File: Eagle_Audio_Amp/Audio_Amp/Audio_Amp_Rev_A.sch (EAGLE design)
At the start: 1 part, among them IC1 LM386M-1

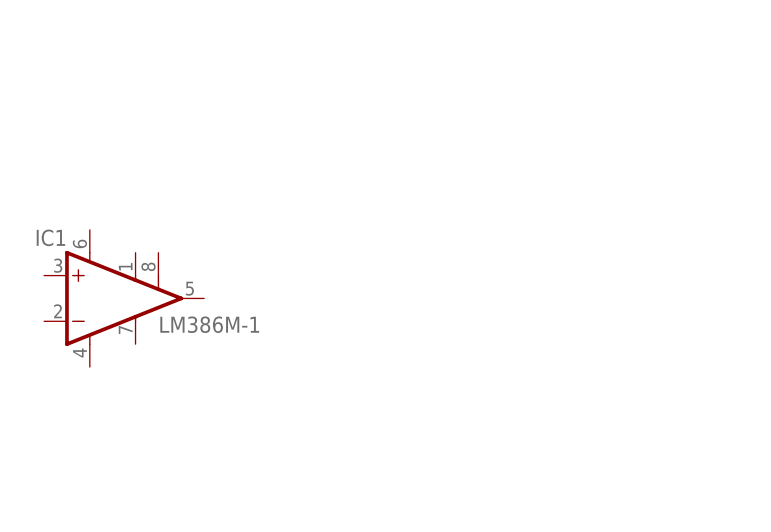
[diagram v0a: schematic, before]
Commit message: Add basic LM386 circuit with bass boost
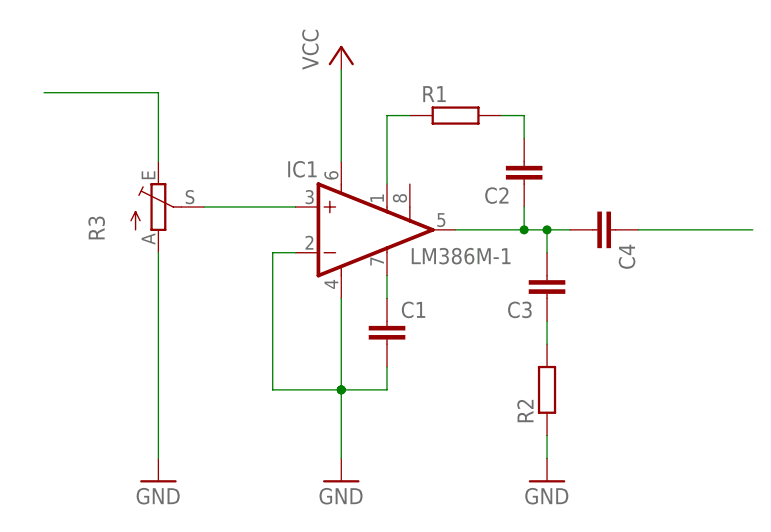
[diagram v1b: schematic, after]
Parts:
- added C1, C2, C3, C4: (no value), rcl:C-EUC0805
- added R1, R2: (no value), rcl:R-EU_R0805
- added R3: (no value), pot:TRIM_EU-CIP20C-6MM
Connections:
- new net GND: C1.2, IC1.-IN, IC1.GND, R2.1, R3.A
- new net N$1: C1.1, IC1.BYPASS
- new net N$2: IC1.+IN, R3.S
- new net N$3: C2.1, C3.2, C4.2, IC1.OUT
- new net N$4: IC1.GAIN@1, R1.1
- new net N$5: C2.2, R1.2
- new net N$6: C3.1, R2.2
- new net N$7: C4.1
- new net N$8: R3.E
- new net VCC: IC1.VS
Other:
- moved on the sheet: IC1
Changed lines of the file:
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@@
 <setting verticaltext="up"/>
 </settings>
-<grid distance="0.1" unitdist="inch" unit="inch" style="lines" multiple="1" display="no" altdistance="0.01" altunitdist="inch" altunit="inch"/>
+<grid distance="0.1" unitdist="inch" unit="inch" style="lines" multiple="1" display="yes" altdistance="0.01" altunitdist="inch" altunit="inch"/>
 <layers>
 <layer number="1" name="Top" color="4" fill="1" visible="no" active="no"/>
@@
 <parts>
 <part name="IC1" library="linear" deviceset="LM386?-*" device="M" technology="1"/>
+<part name="R1" library="rcl" deviceset="R-EU_" device="R0805"/>
+<part name="C1" library="rcl" deviceset="C-EU" device="C0805"/>
+<part name="C2" library="rcl" deviceset="C-EU" device="C0805"/>
+<part name="C3" library="rcl" deviceset="C-EU" device="C0805"/>
+<part name="C4" library="rcl" deviceset="C-EU" device="C0805"/>
+<part name="GND1" library="supply1" deviceset="GND" device=""/>
+<part name="GND2" library="supply1" deviceset="GND" device=""/>
+<part name="P+1" library="supply1" deviceset="VCC" device=""/>
+<part name="R3" library="pot" deviceset="TRIM_EU-" device="CIP20C-6MM"/>
+<part name="R2" library="rcl" deviceset="R-EU_" device="R0805"/>
+<part name="GND4" library="supply1" deviceset="GND" device=""/>
 </parts>
 <sheets>
@@
 </plain>
 <instances>
-<instance part="IC1" gate="G$1" x="63.5" y="48.26"/>
+<instance part="IC1" gate="G$1" x="91.44" y="55.88"/>
+<instance part="R1" gate="G$1" x="101.6" y="68.58"/>
+<instance part="C1" gate="G$1" x="93.98" y="45.72"/>
+<instance part="C2" gate="G$1" x="109.22" y="60.96" rot="R180"/>
+<instance part="C3" gate="G$1" x="111.76" y="48.26" rot="R180"/>
+<instance part="C4" gate="G$1" x="119.38" y="55.88" rot="R270"/>
+<instance part="GND1" gate="1" x="68.58" y="27.94"/>
+<instance part="GND2" gate="1" x="88.9" y="27.94"/>
+<instance part="P+1" gate="VCC" x="88.9" y="76.2"/>
+<instance part="R3" gate="1" x="68.58" y="58.42"/>
+<instance part="R2" gate="G$1" x="111.76" y="38.1" rot="R90"/>
+<instance part="GND4" gate="1" x="111.76" y="27.94"/>
 </instances>
 <busses>
 </busses>
 <nets>
+<net name="N$2" class="0">
+<segment>
+<pinref part="IC1" gate="G$1" pin="+IN"/>
+<wire x1="83.82" y1="58.42" x2="73.66" y2="58.42" width="0.1524" layer="91"/>
+<pinref part="R3" gate="1" pin="S"/>
+</segment>
+</net>
+<net name="GND" class="0">
+<segment>
+<pinref part="IC1" gate="G$1" pin="-IN"/>
+<wire x1="83.82" y1="53.34" x2="81.28" y2="53.34" width="0.1524" layer="91"/>
+<wire x1="81.28" y1="53.34" x2="81.28" y2="38.1" width="0.1524" layer="91"/>
+<wire x1="81.28" y1="38.1" x2="88.9" y2="38.1" width="0.1524" layer="91"/>
+<pinref part="IC1" gate="G$1" pin="GND"/>
+<wire x1="88.9" y1="38.1" x2="88.9" y2="48.26" width="0.1524" layer="91"/>
+<pinref part="GND2" gate="1" pin="GND"/>
+<wire x1="88.9" y1="30.48" x2="88.9" y2="38.1" width="0.1524" layer="91"/>
+<junction x="88.9" y="38.1"/>
+<wire x1="93.98" y1="38.1" x2="88.9" y2="38.1" width="0.1524" layer="91"/>
+<junction x="88.9" y="38.1"/>
+<pinref part="C1" gate="G$1" pin="2"/>
+<wire x1="93.98" y1="40.64" x2="93.98" y2="38.1" width="0.1524" layer="91"/>
+</segment>
+<segment>
+<pinref part="R2" gate="G$1" pin="1"/>
+<pinref part="GND4" gate="1" pin="GND"/>
+<wire x1="111.76" y1="33.02" x2="111.76" y2="30.48" width="0.1524" layer="91"/>
+</segment>
+<segment>
+<pinref part="GND1" gate="1" pin="GND"/>
+<pinref part="R3" gate="1" pin="A"/>
+<wire x1="68.58" y1="30.48" x2="68.58" y2="53.34" width="0.1524" layer="91"/>
+</segment>
+</net>
+<net name="N$1" class="0">
+<segment>
+<pinref part="IC1" gate="G$1" pin="BYPASS"/>
+<pinref part="C1" gate="G$1" pin="1"/>
+<wire x1="93.98" y1="50.8" x2="93.98" y2="48.26" width="0.1524" layer="91"/>
+</segment>
+</net>
+<net name="N$3" class="0">
+<segment>
+<pinref part="IC1" gate="G$1" pin="OUT"/>
+<wire x1="101.6" y1="55.88" x2="109.22" y2="55.88" width="0.1524" layer="91"/>
+<pinref part="C2" gate="G$1" pin="1"/>
+<wire x1="109.22" y1="55.88" x2="109.22" y2="58.42" width="0.1524" layer="91"/>
+<pinref part="C4" gate="G$1" pin="2"/>
+<wire x1="109.22" y1="55.88" x2="111.76" y2="55.88" width="0.1524" layer="91"/>
+<junction x="109.22" y="55.88"/>
+<pinref part="C3" gate="G$1" pin="2"/>
+<wire x1="111.76" y1="55.88" x2="114.3" y2="55.88" width="0.1524" layer="91"/>
+<wire x1="111.76" y1="53.34" x2="111.76" y2="55.88" width="0.1524" layer="91"/>
+<junction x="111.76" y="55.88"/>
+</segment>
+</net>
+<net name="N$4" class="0">
+<segment>
+<pinref part="IC1" gate="G$1" pin="GAIN@1"/>
+<wire x1="93.98" y1="60.96" x2="93.98" y2="68.58" width="0.1524" layer="91"/>
+<pinref part="R1" gate="G$1" pin="1"/>
+<wire x1="93.98" y1="68.58" x2="96.52" y2="68.58" width="0.1524" layer="91"/>
+</segment>
+</net>
+<net name="N$5" class="0">
+<segment>
+<pinref part="R1" gate="G$1" pin="2"/>
+<wire x1="106.68" y1="68.58" x2="109.22" y2="68.58" width="0.1524" layer="91"/>
+<pinref part="C2" gate="G$1" pin="2"/>
+<wire x1="109.22" y1="68.58" x2="109.22" y2="66.04" width="0.1524" layer="91"/>
+</segment>
+</net>
+<net name="N$6" class="0">
+<segment>
+<pinref part="C3" gate="G$1" pin="1"/>
+<pinref part="R2" gate="G$1" pin="2"/>
+<wire x1="111.76" y1="45.72" x2="111.76" y2="43.18" width="0.1524" layer="91"/>
+</segment>
+</net>
+<net name="VCC" class="0">
+<segment>
+<pinref part="IC1" gate="G$1" pin="VS"/>
+<pinref part="P+1" gate="VCC" pin="VCC"/>
+<wire x1="88.9" y1="63.5" x2="88.9" y2="73.66" width="0.1524" layer="91"/>
+</segment>
+</net>
+<net name="N$7" class="0">
+<segment>
+<pinref part="C4" gate="G$1" pin="1"/>
+<wire x1="121.92" y1="55.88" x2="134.62" y2="55.88" width="0.1524" layer="91"/>
+</segment>
+</net>
+<net name="N$8" class="0">
+<segment>
+<pinref part="R3" gate="1" pin="E"/>
+<wire x1="68.58" y1="63.5" x2="68.58" y2="71.12" width="0.1524" layer="91"/>
+<wire x1="68.58" y1="71.12" x2="55.88" y2="71.12" width="0.1524" layer="91"/>
+</segment>
+</net>
 </nets>
 </sheet>

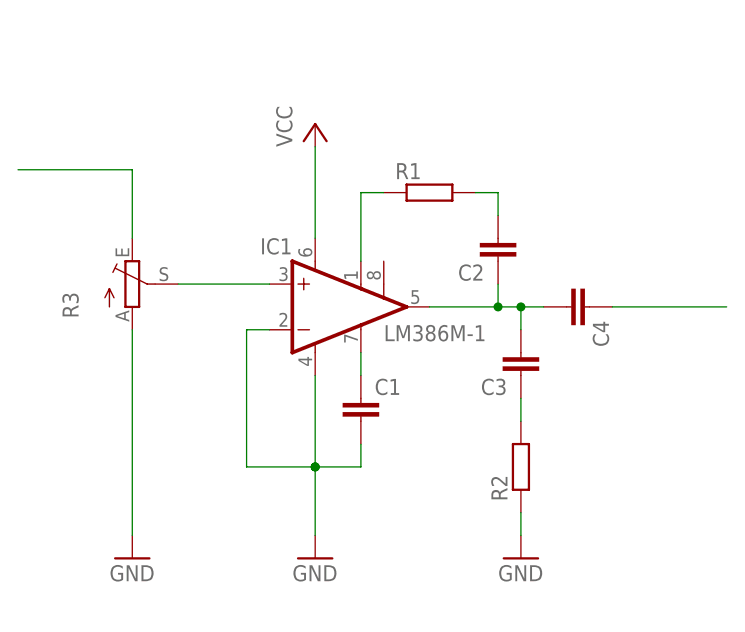
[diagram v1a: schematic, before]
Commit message: Add amplifier gain to circuit and component values
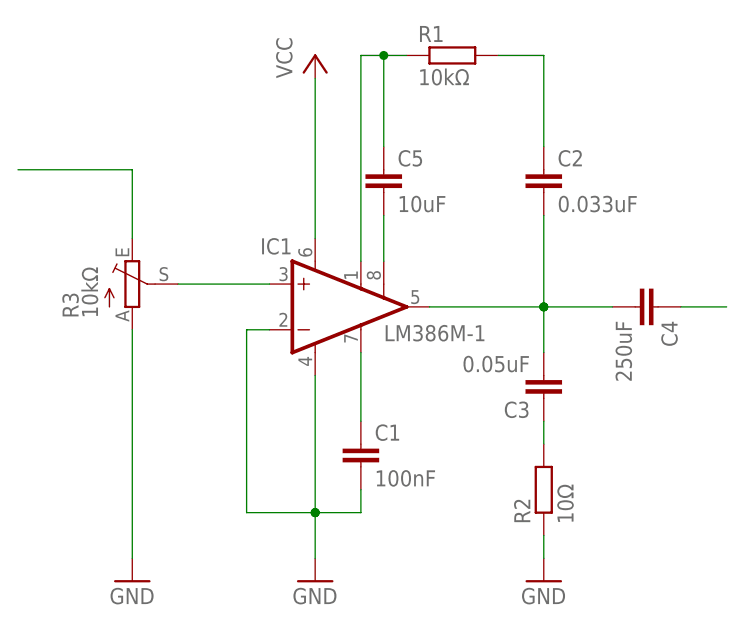
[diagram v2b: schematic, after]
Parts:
- added C5: 10uF, rcl:C-EUC0805
- C1: value (none) -> 100nF
- C2: value (none) -> 0.033uF
- C3: value (none) -> 0.05uF
- C4: value (none) -> 250uF
- R1, R3: value (none) -> 10kΩ
- R2: value (none) -> 10Ω
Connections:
- new net N$9: C5.2, IC1.GAIN@2
- net N$3: now also C2.2; no longer C2.1
- net N$4: now also C5.1
- net N$5: now also C2.1; no longer C2.2
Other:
- moved on the sheet: C1, C2, C3, C4, R1, R2
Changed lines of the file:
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@@
 <parts>
 <part name="IC1" library="linear" deviceset="LM386?-*" device="M" technology="1"/>
-<part name="R1" library="rcl" deviceset="R-EU_" device="R0805"/>
-<part name="C1" library="rcl" deviceset="C-EU" device="C0805"/>
-<part name="C2" library="rcl" deviceset="C-EU" device="C0805"/>
-<part name="C3" library="rcl" deviceset="C-EU" device="C0805"/>
-<part name="C4" library="rcl" deviceset="C-EU" device="C0805"/>
+<part name="R1" library="rcl" deviceset="R-EU_" device="R0805" value="10kΩ"/>
+<part name="C1" library="rcl" deviceset="C-EU" device="C0805" value="100nF"/>
+<part name="C2" library="rcl" deviceset="C-EU" device="C0805" value="0.033uF"/>
+<part name="C3" library="rcl" deviceset="C-EU" device="C0805" value="0.05uF"/>
+<part name="C4" library="rcl" deviceset="C-EU" device="C0805" value="250uF"/>
 <part name="GND1" library="supply1" deviceset="GND" device=""/>
 <part name="GND2" library="supply1" deviceset="GND" device=""/>
 <part name="P+1" library="supply1" deviceset="VCC" device=""/>
-<part name="R3" library="pot" deviceset="TRIM_EU-" device="CIP20C-6MM"/>
-<part name="R2" library="rcl" deviceset="R-EU_" device="R0805"/>
+<part name="R3" library="pot" deviceset="TRIM_EU-" device="CIP20C-6MM" value="10kΩ"/>
+<part name="R2" library="rcl" deviceset="R-EU_" device="R0805" value="10Ω"/>
 <part name="GND4" library="supply1" deviceset="GND" device=""/>
+<part name="C5" library="rcl" deviceset="C-EU" device="C0805" value="10uF"/>
 </parts>
 <sheets>
@@
 <instances>
 <instance part="IC1" gate="G$1" x="91.44" y="55.88"/>
-<instance part="R1" gate="G$1" x="101.6" y="68.58"/>
-<instance part="C1" gate="G$1" x="93.98" y="45.72"/>
-<instance part="C2" gate="G$1" x="109.22" y="60.96" rot="R180"/>
-<instance part="C3" gate="G$1" x="111.76" y="48.26" rot="R180"/>
-<instance part="C4" gate="G$1" x="119.38" y="55.88" rot="R270"/>
-<instance part="GND1" gate="1" x="68.58" y="27.94"/>
-<instance part="GND2" gate="1" x="88.9" y="27.94"/>
-<instance part="P+1" gate="VCC" x="88.9" y="76.2"/>
+<instance part="R1" gate="G$1" x="104.14" y="83.82"/>
+<instance part="C1" gate="G$1" x="93.98" y="40.64"/>
+<instance part="C2" gate="G$1" x="114.3" y="71.12"/>
+<instance part="C3" gate="G$1" x="114.3" y="45.72" rot="R180"/>
+<instance part="C4" gate="G$1" x="127" y="55.88" rot="R270"/>
+<instance part="GND1" gate="1" x="68.58" y="25.4"/>
+<instance part="GND2" gate="1" x="88.9" y="25.4"/>
+<instance part="P+1" gate="VCC" x="88.9" y="83.82"/>
 <instance part="R3" gate="1" x="68.58" y="58.42"/>
-<instance part="R2" gate="G$1" x="111.76" y="38.1" rot="R90"/>
-<instance part="GND4" gate="1" x="111.76" y="27.94"/>
+<instance part="R2" gate="G$1" x="114.3" y="35.56" rot="R90"/>
+<instance part="GND4" gate="1" x="114.3" y="25.4"/>
+<instance part="C5" gate="G$1" x="96.52" y="71.12"/>
 </instances>
 <busses>
@@
 <pinref part="IC1" gate="G$1" pin="-IN"/>
 <wire x1="83.82" y1="53.34" x2="81.28" y2="53.34" width="0.1524" layer="91"/>
-<wire x1="81.28" y1="53.34" x2="81.28" y2="38.1" width="0.1524" layer="91"/>
-<wire x1="81.28" y1="38.1" x2="88.9" y2="38.1" width="0.1524" layer="91"/>
+<wire x1="81.28" y1="53.34" x2="81.28" y2="33.02" width="0.1524" layer="91"/>
+<wire x1="81.28" y1="33.02" x2="88.9" y2="33.02" width="0.1524" layer="91"/>
 <pinref part="IC1" gate="G$1" pin="GND"/>
-<wire x1="88.9" y1="38.1" x2="88.9" y2="48.26" width="0.1524" layer="91"/>
+<wire x1="88.9" y1="33.02" x2="88.9" y2="48.26" width="0.1524" layer="91"/>
 <pinref part="GND2" gate="1" pin="GND"/>
-<wire x1="88.9" y1="30.48" x2="88.9" y2="38.1" width="0.1524" layer="91"/>
-<junction x="88.9" y="38.1"/>
-<wire x1="93.98" y1="38.1" x2="88.9" y2="38.1" width="0.1524" layer="91"/>
-<junction x="88.9" y="38.1"/>
+<wire x1="88.9" y1="27.94" x2="88.9" y2="33.02" width="0.1524" layer="91"/>
+<junction x="88.9" y="33.02"/>
+<wire x1="93.98" y1="33.02" x2="88.9" y2="33.02" width="0.1524" layer="91"/>
+<junction x="88.9" y="33.02"/>
 <pinref part="C1" gate="G$1" pin="2"/>
-<wire x1="93.98" y1="40.64" x2="93.98" y2="38.1" width="0.1524" layer="91"/>
+<wire x1="93.98" y1="35.56" x2="93.98" y2="33.02" width="0.1524" layer="91"/>
 </segment>
 <segment>
 <pinref part="R2" gate="G$1" pin="1"/>
 <pinref part="GND4" gate="1" pin="GND"/>
-<wire x1="111.76" y1="33.02" x2="111.76" y2="30.48" width="0.1524" layer="91"/>
+<wire x1="114.3" y1="30.48" x2="114.3" y2="27.94" width="0.1524" layer="91"/>
 </segment>
 <segment>
 <pinref part="GND1" gate="1" pin="GND"/>
 <pinref part="R3" gate="1" pin="A"/>
-<wire x1="68.58" y1="30.48" x2="68.58" y2="53.34" width="0.1524" layer="91"/>
+<wire x1="68.58" y1="27.94" x2="68.58" y2="53.34" width="0.1524" layer="91"/>
 </segment>
 </net>
@@
 <pinref part="IC1" gate="G$1" pin="BYPASS"/>
 <pinref part="C1" gate="G$1" pin="1"/>
-<wire x1="93.98" y1="50.8" x2="93.98" y2="48.26" width="0.1524" layer="91"/>
+<wire x1="93.98" y1="50.8" x2="93.98" y2="43.18" width="0.1524" layer="91"/>
 </segment>
 </net>
@@
 <segment>
 <pinref part="IC1" gate="G$1" pin="OUT"/>
-<wire x1="101.6" y1="55.88" x2="109.22" y2="55.88" width="0.1524" layer="91"/>
-<pinref part="C2" gate="G$1" pin="1"/>
-<wire x1="109.22" y1="55.88" x2="109.22" y2="58.42" width="0.1524" layer="91"/>
+<wire x1="101.6" y1="55.88" x2="114.3" y2="55.88" width="0.1524" layer="91"/>
 <pinref part="C4" gate="G$1" pin="2"/>
-<wire x1="109.22" y1="55.88" x2="111.76" y2="55.88" width="0.1524" layer="91"/>
-<junction x="109.22" y="55.88"/>
+<junction x="114.3" y="55.88"/>
 <pinref part="C3" gate="G$1" pin="2"/>
-<wire x1="111.76" y1="55.88" x2="114.3" y2="55.88" width="0.1524" layer="91"/>
-<wire x1="111.76" y1="53.34" x2="111.76" y2="55.88" width="0.1524" layer="91"/>
-<junction x="111.76" y="55.88"/>
+<wire x1="114.3" y1="55.88" x2="121.92" y2="55.88" width="0.1524" layer="91"/>
+<wire x1="114.3" y1="50.8" x2="114.3" y2="55.88" width="0.1524" layer="91"/>
+<junction x="114.3" y="55.88"/>
+<pinref part="C2" gate="G$1" pin="2"/>
+<wire x1="114.3" y1="55.88" x2="114.3" y2="66.04" width="0.1524" layer="91"/>
 </segment>
 </net>
@@
 <segment>
 <pinref part="IC1" gate="G$1" pin="GAIN@1"/>
-<wire x1="93.98" y1="60.96" x2="93.98" y2="68.58" width="0.1524" layer="91"/>
+<wire x1="93.98" y1="60.96" x2="93.98" y2="83.82" width="0.1524" layer="91"/>
 <pinref part="R1" gate="G$1" pin="1"/>
-<wire x1="93.98" y1="68.58" x2="96.52" y2="68.58" width="0.1524" layer="91"/>
+<wire x1="93.98" y1="83.82" x2="96.52" y2="83.82" width="0.1524" layer="91"/>
+<pinref part="C5" gate="G$1" pin="1"/>
+<wire x1="96.52" y1="83.82" x2="99.06" y2="83.82" width="0.1524" layer="91"/>
+<wire x1="96.52" y1="73.66" x2="96.52" y2="83.82" width="0.1524" layer="91"/>
+<junction x="96.52" y="83.82"/>
 </segment>
 </net>
@@
 <segment>
 <pinref part="R1" gate="G$1" pin="2"/>
-<wire x1="106.68" y1="68.58" x2="109.22" y2="68.58" width="0.1524" layer="91"/>
-<pinref part="C2" gate="G$1" pin="2"/>
-<wire x1="109.22" y1="68.58" x2="109.22" y2="66.04" width="0.1524" layer="91"/>
+<wire x1="109.22" y1="83.82" x2="114.3" y2="83.82" width="0.1524" layer="91"/>
+<pinref part="C2" gate="G$1" pin="1"/>
+<wire x1="114.3" y1="73.66" x2="114.3" y2="83.82" width="0.1524" layer="91"/>
 </segment>
 </net>
@@
 <pinref part="C3" gate="G$1" pin="1"/>
 <pinref part="R2" gate="G$1" pin="2"/>
-<wire x1="111.76" y1="45.72" x2="111.76" y2="43.18" width="0.1524" layer="91"/>
+<wire x1="114.3" y1="43.18" x2="114.3" y2="40.64" width="0.1524" layer="91"/>
 </segment>
 </net>
@@
 <pinref part="IC1" gate="G$1" pin="VS"/>
 <pinref part="P+1" gate="VCC" pin="VCC"/>
-<wire x1="88.9" y1="63.5" x2="88.9" y2="73.66" width="0.1524" layer="91"/>
+<wire x1="88.9" y1="63.5" x2="88.9" y2="81.28" width="0.1524" layer="91"/>
 </segment>
 </net>
@@
 <segment>
 <pinref part="C4" gate="G$1" pin="1"/>
-<wire x1="121.92" y1="55.88" x2="134.62" y2="55.88" width="0.1524" layer="91"/>
+<wire x1="129.54" y1="55.88" x2="134.62" y2="55.88" width="0.1524" layer="91"/>
 </segment>
 </net>
@@
 </segment>
 </net>
+<net name="N$9" class="0">
+<segment>
+<pinref part="IC1" gate="G$1" pin="GAIN@2"/>
+<pinref part="C5" gate="G$1" pin="2"/>
+<wire x1="96.52" y1="60.96" x2="96.52" y2="66.04" width="0.1524" layer="91"/>
+</segment>
+</net>
